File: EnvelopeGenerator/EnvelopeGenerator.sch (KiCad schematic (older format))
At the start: 35 parts

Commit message: Finished Schematic
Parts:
- removed RV? (x3): R_POT, symbol Device:R_POT
- added C?: 4n7, symbol Device:C
- added C? (x2): 0.1u, symbol Device:C
- added C? (x2): 100u, symbol Device:CP
- added C?: 10u, symbol Device:CP
- added D? (x4): 1N4001, Diode_THT:D_DO-35_SOD27_P7.62mm_Horizontal, symbol Diode:1N4148
- added D?: 1N4148, Diode_THT:D_DO-35_SOD27_P7.62mm_Horizontal, symbol Diode:1N4148
- added R? (x2): 47k, symbol Device:R
- added R?: 12k, symbol Device:R
- added RV? (x3): 10k, symbol Device:R_POT
- C?: value CP -> 10u
- R? (x3): value R -> 200
- R?: value R -> 15k
- R? (x3): value R -> 12k
- R?: value R -> 20k
- RV?: value R_POT -> 10k
- gave numbers to parts that had none: 1
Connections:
- net +12V: now also C?.1, U?.14 (VCC), U?.3 (OUT), C?.2, D?.1 (K), D?.2 (A)
- net +15V: now also J?.1 (Pin_1), U?.1 (IN), C?.1, D?.1 (K), R?.2, RV?.1, RV?.1, RV?.1
- net -12V: now also U?.3 (VO), U?.7 (VEE), C?.1, C?.2, D?.1 (K), D?.2 (A)
- net -15V: now also J?.3 (Pin_3), U?.2 (VI), C?.2, D?.2 (A), RV?.3, RV?.3, RV?.3
- net GATE: now also J?.5 (Pin_5), D?.2 (A); no longer C?.2, R?.1, U?.4 (GATE)
- net GND: now also C?.2, J?.2 (Pin_2), R?.1, U?.1 (GND), U?.1 (GND), U?.2 (GND), C?.1, C?.1, C?.1, C?.1, C?.2, C?.2, D?.1 (K), D?.2 (A), R?.1
- net at U?.3 (VE1): now also U?.5 (VC1), U?.6 (II1), R?.2
- net at U?.8 (VREF): now also C?.2
- net SIG_OUT: now reaches R?.2, U?.13 (IO2)
- net SIG_OUT: now also J?.4 (Pin_4)
- net at U?.9 (II2): now also R?.2
- net at R?.2: now also RV?.2 (x3)
- net at J?.1 (Pin_1): now also C?.2, R?.1, R?.2, U?.4 (GATE), D?.1 (K)
- net at J?.2 (Pin_2): now also R?.1
- new net SIG_IN: R?.1
- no-connect marks 0 -> 5
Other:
- note added: "ADSR Voltage Generator"
- note added: "Diode prevents Sustain \nlevel from being above\nAttack Level"
- note added: "Manual Trigger"
- note added: "VCA"
- note added: "±12 Supply"
- moved on the sheet: C?, D?, J?, R?, RV?, U?, U?A, U?B

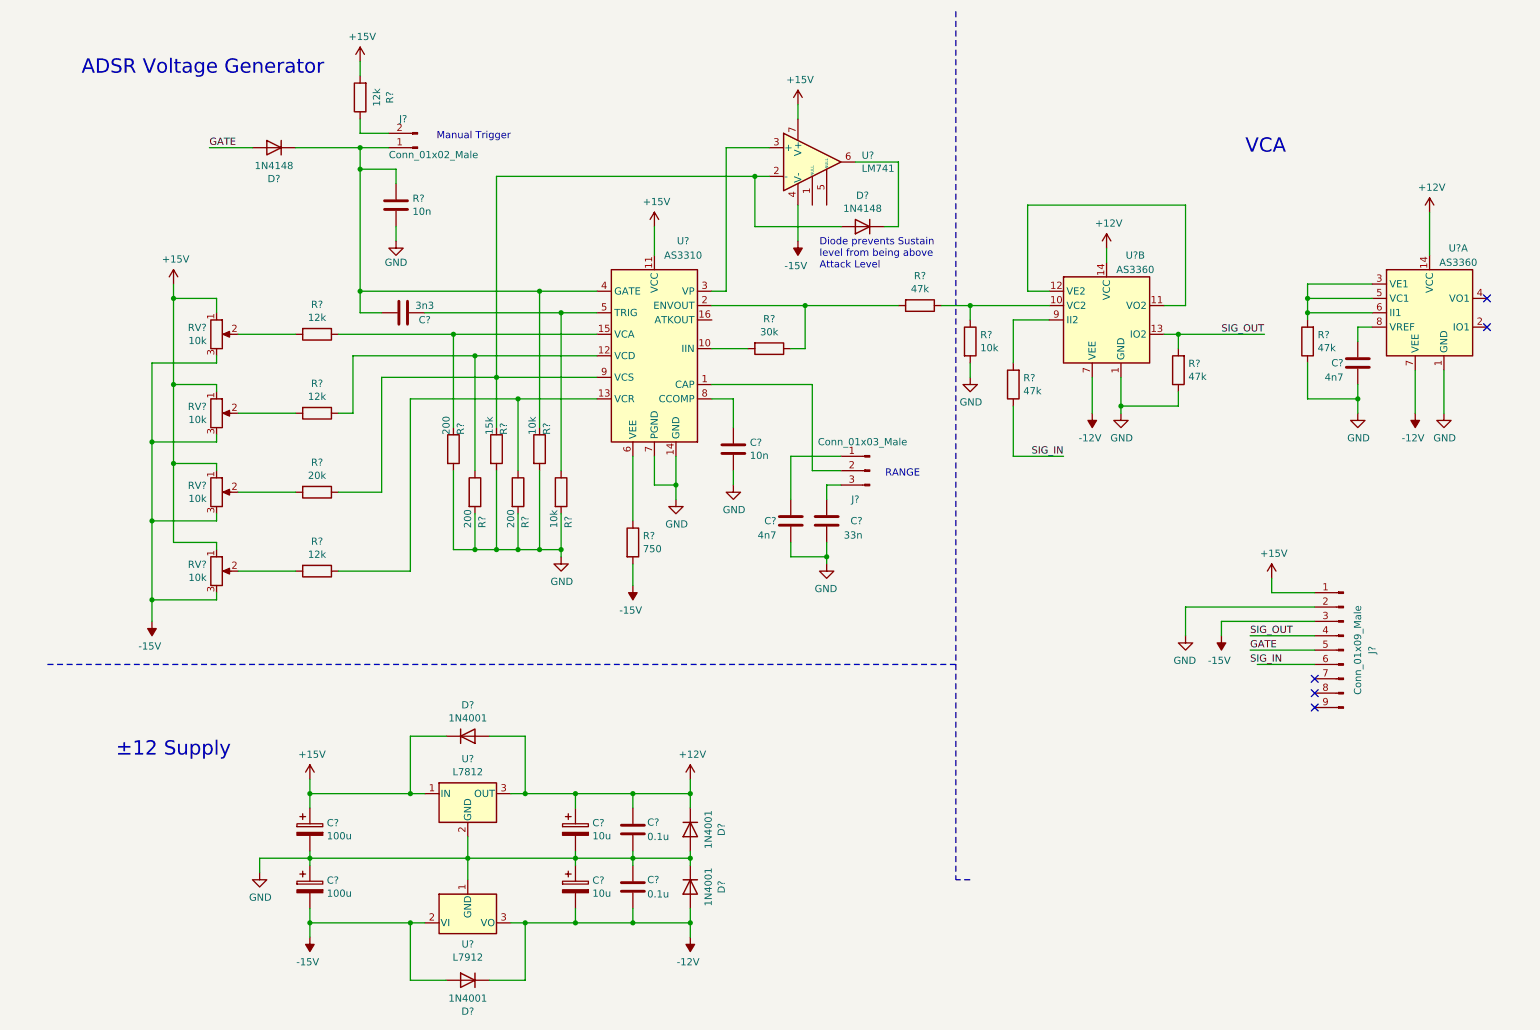
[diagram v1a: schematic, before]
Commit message: Finished PCB routing, minor schematic fixes Also: * Generated board rendering * Exported schematic PDF * Added README
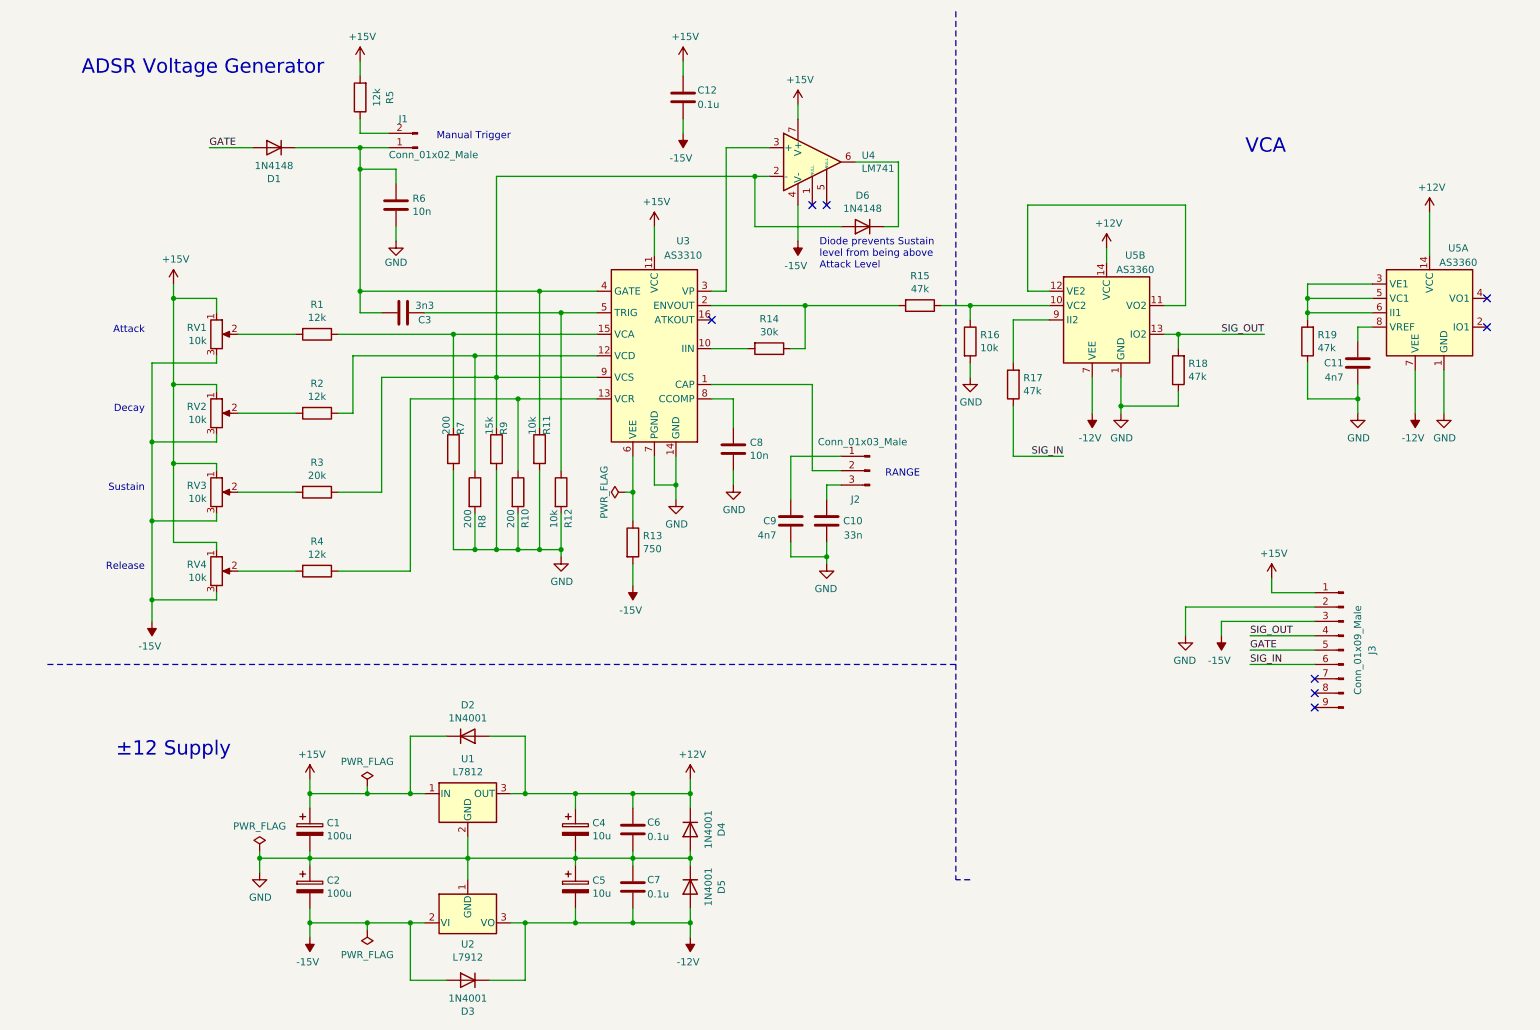
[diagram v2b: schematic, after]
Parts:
- added C12: 0.1u, Capacitor_THT:C_Disc_D4.3mm_W1.9mm_P5.00mm, symbol Device:C
- C1, C2, C4, C5: renamed from C?; footprint (none) -> Capacitor_THT:CP_Radial_D8.0mm_P3.50mm
- C10, C11, C3, C6, C7, C8, C9: renamed from C?; footprint (none) -> Capacitor_THT:C_Disc_D4.3mm_W1.9mm_P5.00mm
- J1: renamed from J?; footprint (none) -> Connector_PinHeader_2.54mm:PinHeader_1x02_P2.54mm_Vertical
- J2: renamed from J?; footprint (none) -> Connector_PinHeader_2.54mm:PinHeader_1x03_P2.54mm_Vertical
- J3: renamed from J?; footprint (none) -> Connector_PinHeader_2.54mm:PinHeader_1x09_P2.54mm_Vertical
- R1, R10, R11, R12, R14, R15, R16, R17, R18, R19, R2, R3, R4, R5, R6, R7, R8, R9: renamed from R?; footprint (none) -> Resistor_THT:R_Axial_DIN0204_L3.6mm_D1.6mm_P5.08mm_Horizontal
- R13: renamed from R?; footprint (none) -> Resistor_THT:R_Axial_DIN0414_L11.9mm_D4.5mm_P5.08mm_Vertical
- RV1, RV2, RV3, RV4: renamed from RV?; footprint (none) -> Potentiometer_THT:Potentiometer_Piher_PC-16_Single_Horizontal
- U1, U2: renamed from U?; footprint (none) -> Package_TO_SOT_THT:TO-220-3_Vertical
- U3: renamed from U?; footprint (none) -> Package_DIP:DIP-16_W7.62mm_Socket_LongPads
- U4: renamed from U?; footprint (none) -> Package_DIP:DIP-8_W7.62mm_Socket_LongPads
- U5: renamed from U?; footprint (none) -> Package_DIP:DIP-14_W7.62mm_Socket_LongPads
- gave numbers to parts that had none: 6
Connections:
- net +15V: now also C12.2
- net -15V: now also C12.1
- net SIG_IN: now also J3.6 (Pin_6)
- net SIG_OUT: now also U5.13 (IO2); no longer U5.13 (IO2)
- net at C11.2: now also U5.8 (VREF); no longer U5.8 (VREF)
- net at R15.1, R16.1: now also U5.10 (VC2); no longer U5.10 (VC2)
- net at R17.2: now also U5.9 (II2); no longer U5.9 (II2)
- new net: U5.11 (VO2), U5.12 (VE2)
- new net: R19.2, U5.3 (VE1), U5.5 (VC1), U5.6 (II1)
- no-connect marks 5 -> 8
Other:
- note added: "Attack"
- note added: "Decay"
- note added: "Release"
- note added: "Sustain"

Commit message: Designed and routed Envelope Filter PCB Also: * Finished Envelope Filter schematic * Exported cool RTX board render * Exported PDF of schematic * Began work on README
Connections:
- net +15V: no longer RV3.1
- net -15V: now also RV3.1; no longer RV3.3
- net GND: now also RV3.3
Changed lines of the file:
@@
 	-1   0    0    1
-$EndComp
-$Comp
-L Device:R_POT RV1
-U 1 1 5FE2ACDE
-P 1700 2750
-F 0 "RV1" H 1631 2796 50  0000 R CNN
-F 1 "10k" H 1631 2705 50  0000 R CNN
-F 2 "Potentiometer_THT:Potentiometer_Piher_PC-16_Single_Horizontal" H 1700 2750 50  0001 C CNN
-F 3 "~" H 1700 2750 50  0001 C CNN
-	1    1700 2750
-	1    0    0    -1
 $EndComp
 Wire Wire Line
@@
 	1700 3100 1700 3150
 Connection ~ 1400 2500
-Wire Wire Line
-	1400 3100 1400 3650
-Wire Wire Line
-	1700 3650 1700 3700
 Connection ~ 1400 3100
 Wire Wire Line
-	1400 3650 1400 4200
-Wire Wire Line
 	1700 4200 1700 4250
-Connection ~ 1400 3650
 Wire Wire Line
 	1700 4600 1700 4550
@@
 	2550 4400 3050 4400
 $Comp
-L Device:R_POT RV2
-U 1 1 5FDA4965
-P 1700 3300
-F 0 "RV2" H 1631 3346 50  0000 R CNN
-F 1 "10k" H 1631 3255 50  0000 R CNN
-F 2 "Potentiometer_THT:Potentiometer_Piher_PC-16_Single_Horizontal" H 1700 3300 50  0001 C CNN
-F 3 "~" H 1700 3300 50  0001 C CNN
-	1    1700 3300
-	1    0    0    -1
-$EndComp
-$Comp
 L Device:R_POT RV3
 U 1 1 5FDA4F64
@@
 F 3 "~" H 1700 3850 50  0001 C CNN
 	1    1700 3850
-	1    0    0    -1
-$EndComp
-$Comp
-L Device:R_POT RV4
-U 1 1 5FDA5552
-P 1700 4400
-F 0 "RV4" H 1631 4446 50  0000 R CNN
-F 1 "10k" H 1631 4355 50  0000 R CNN
-F 2 "Potentiometer_THT:Potentiometer_Piher_PC-16_Single_Horizontal" H 1700 4400 50  0001 C CNN
-F 3 "~" H 1700 4400 50  0001 C CNN
-	1    1700 4400
-	1    0    0    -1
+	1    0    0    1
 $EndComp
 Wire Wire Line
@@
 Wire Wire Line
 	1250 3500 1700 3500
-Wire Wire Line
-	1400 3650 1700 3650
 Wire Wire Line
 	1250 4050 1700 4050
@@
 Wire Wire Line
 	4200 5950 4600 5950
+$Comp
+L power:GND #PWR0131
+U 1 1 606E9E6B
+P 1950 3600
+F 0 "#PWR0131" H 1950 3350 50  0001 C CNN
+F 1 "GND" H 1955 3427 50  0000 C CNN
+F 2 "" H 1950 3600 50  0001 C CNN
+F 3 "" H 1950 3600 50  0001 C CNN
+	1    1950 3600
+	1    0    0    -1
+$EndComp
+Wire Wire Line
+	1400 3100 1400 4200
+$Comp
+L Device:R_POT RV1
+U 1 1 5FE2ACDE
+P 1700 2750
+F 0 "RV1" H 1631 2796 50  0000 R CNN
+F 1 "10k" H 1631 2705 50  0000 R CNN
+F 2 "Potentiometer_THT:Potentiometer_Piher_PC-16_Single_Horizontal" H 1700 2750 50  0001 C CNN
+F 3 "~" H 1700 2750 50  0001 C CNN
+	1    1700 2750
+	1    0    0    -1
+$EndComp
+$Comp
+L Device:R_POT RV2
+U 1 1 5FDA4965
+P 1700 3300
+F 0 "RV2" H 1631 3346 50  0000 R CNN
+F 1 "10k" H 1631 3255 50  0000 R CNN
+F 2 "Potentiometer_THT:Potentiometer_Piher_PC-16_Single_Horizontal" H 1700 3300 50  0001 C CNN
+F 3 "~" H 1700 3300 50  0001 C CNN
+	1    1700 3300
+	1    0    0    -1
+$EndComp
+$Comp
+L Device:R_POT RV4
+U 1 1 5FDA5552
+P 1700 4400
+F 0 "RV4" H 1631 4446 50  0000 R CNN
+F 1 "10k" H 1631 4355 50  0000 R CNN
+F 2 "Potentiometer_THT:Potentiometer_Piher_PC-16_Single_Horizontal" H 1700 4400 50  0001 C CNN
+F 3 "~" H 1700 4400 50  0001 C CNN
+	1    1700 4400
+	1    0    0    -1
+$EndComp
+Wire Wire Line
+	1700 3550 1950 3550
+Wire Wire Line
+	1950 3550 1950 3600
+Wire Wire Line
+	1700 3550 1700 3700
 $EndSCHEMATC

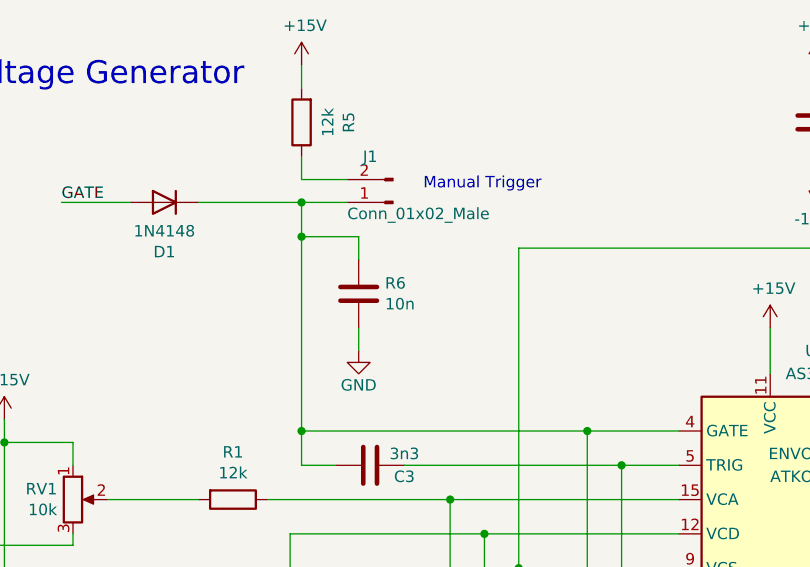
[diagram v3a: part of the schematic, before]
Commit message: Updated PCB annotations
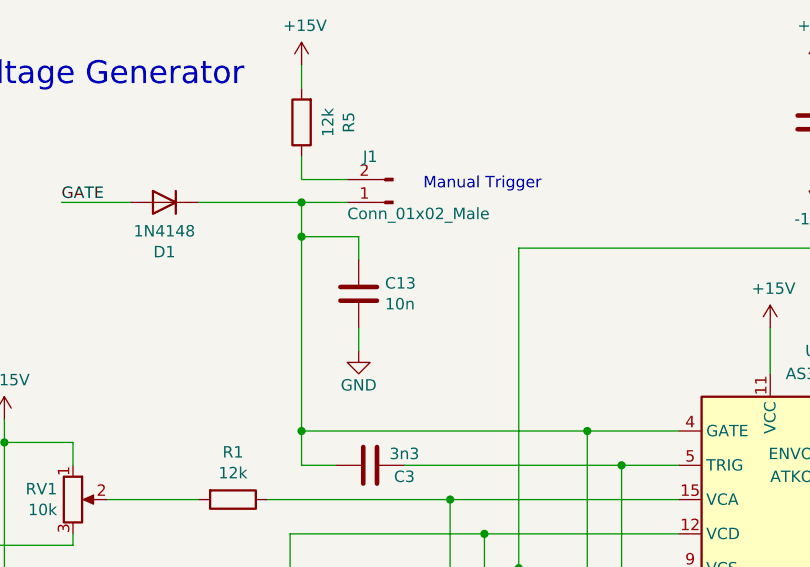
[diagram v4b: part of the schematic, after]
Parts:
- renumbered R6 to C13
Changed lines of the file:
@@
 $EndComp
 $Comp
-L Device:C R6
+L Device:C C13
 U 1 1 5FE1841F
 P 2950 1850
-F 0 "R6" H 2835 1804 50  0000 R CNN
+F 0 "C13" H 2835 1804 50  0000 R CNN
 F 1 "10n" H 2835 1895 50  0000 R CNN
 F 2 "Resistor_THT:R_Axial_DIN0204_L3.6mm_D1.6mm_P5.08mm_Horizontal" H 2988 1700 50  0001 C CNN
